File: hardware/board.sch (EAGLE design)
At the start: 45 parts, among them IC1 0915BM15A0001, J1 U.FL, U3 BLE113-A, X1 26MHz 10pF 10ppm -20C +70C, X3 MINI-USB-UX60-MB-5ST

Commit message: Update parts for 24MHz in schematic and BOM
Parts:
- C5, C6: value 27pF -> 11pF
- X1: value 26MHz 10pF 10ppm -20C +70C -> 24MHz 8pF 10ppm -20C +70C
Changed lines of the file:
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@@
 <?xml version="1.0" encoding="utf-8"?>
 <!DOCTYPE eagle SYSTEM "eagle.dtd">
-<eagle version="7.1.0">
+<eagle version="7.4.0">
 <drawing>
 <settings>
@@
 <parts>
 <part name="CC1110" library="parts" deviceset="CC1110" device=""/>
-<part name="X1" library="cts_crystal" deviceset="CTS_32X25_SMD" device="" value="26MHz 10pF 10ppm -20C +70C"/>
+<part name="X1" library="cts_crystal" deviceset="CTS_32X25_SMD" device="" value="24MHz 8pF 10ppm -20C +70C"/>
 <part name="C1" library="rcl" deviceset="C-EU" device="C0402" value="100nF"/>
 <part name="SUPPLY4" library="supply2" deviceset="GND" device=""/>
@@
 <part name="J1" library="SparkFun-Connectors" deviceset="U.FL" device="" value="U.FL"/>
 <part name="U3" library="sf-bluegiga" deviceset="BLE113" device="-A"/>
-<part name="C5" library="rcl" deviceset="C-EU" device="C0402K" value="27pF"/>
-<part name="C6" library="rcl" deviceset="C-EU" device="C0402K" value="27pF"/>
+<part name="C5" library="rcl" deviceset="C-EU" device="C0402K" value="11pF"/>
+<part name="C6" library="rcl" deviceset="C-EU" device="C0402K" value="11pF"/>
 <part name="GND15" library="supply1" deviceset="GND" device=""/>
 <part name="GND16" library="supply1" deviceset="GND" device=""/>

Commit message: Update loading cap specifications to 12pF
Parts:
- C5, C6: value 11pF -> 12pF ±5%
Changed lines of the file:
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@@
 <part name="J1" library="SparkFun-Connectors" deviceset="U.FL" device="" value="U.FL"/>
 <part name="U3" library="sf-bluegiga" deviceset="BLE113" device="-A"/>
-<part name="C5" library="rcl" deviceset="C-EU" device="C0402K" value="11pF"/>
-<part name="C6" library="rcl" deviceset="C-EU" device="C0402K" value="11pF"/>
+<part name="C5" library="rcl" deviceset="C-EU" device="C0402K" value="12pF ±5%"/>
+<part name="C6" library="rcl" deviceset="C-EU" device="C0402K" value="12pF ±5%"/>
 <part name="GND15" library="supply1" deviceset="GND" device=""/>
 <part name="GND16" library="supply1" deviceset="GND" device=""/>

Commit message: Fix decoupling cap; it was an error to have it so big. Also, the Digikey BOM had a mistake for its part number.
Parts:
- C11: value 100uF -> 10uF
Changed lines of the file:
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@@
 <part name="SUPPLY19" library="supply2" deviceset="GND" device=""/>
 <part name="SUPPLY20" library="supply2" deviceset="GND" device=""/>
-<part name="C11" library="rcl" deviceset="C-US" device="C0805K" value="100uF"/>
+<part name="C11" library="rcl" deviceset="C-US" device="C0805K" value="10uF"/>
 <part name="SUPPLY15" library="supply2" deviceset="GND" device=""/>
 <part name="SUPPLY18" library="supply2" deviceset="VDD" device=""/>

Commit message: reduce amount of solder under cc1110, and label board 0.7p for production run
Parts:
- CC1110: device parts:CC1110 -> board:CC1110
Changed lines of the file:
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@@
 </classes>
 <parts>
-<part name="CC1110" library="parts" deviceset="CC1110" device=""/>
+<part name="CC1110" library="board" deviceset="CC1110" device=""/>
 <part name="X1" library="cts_crystal" deviceset="CTS_32X25_SMD" device="" value="24MHz 8pF 10ppm -20C +70C"/>
 <part name="C1" library="rcl" deviceset="C-EU" device="C0402" value="100nF"/>

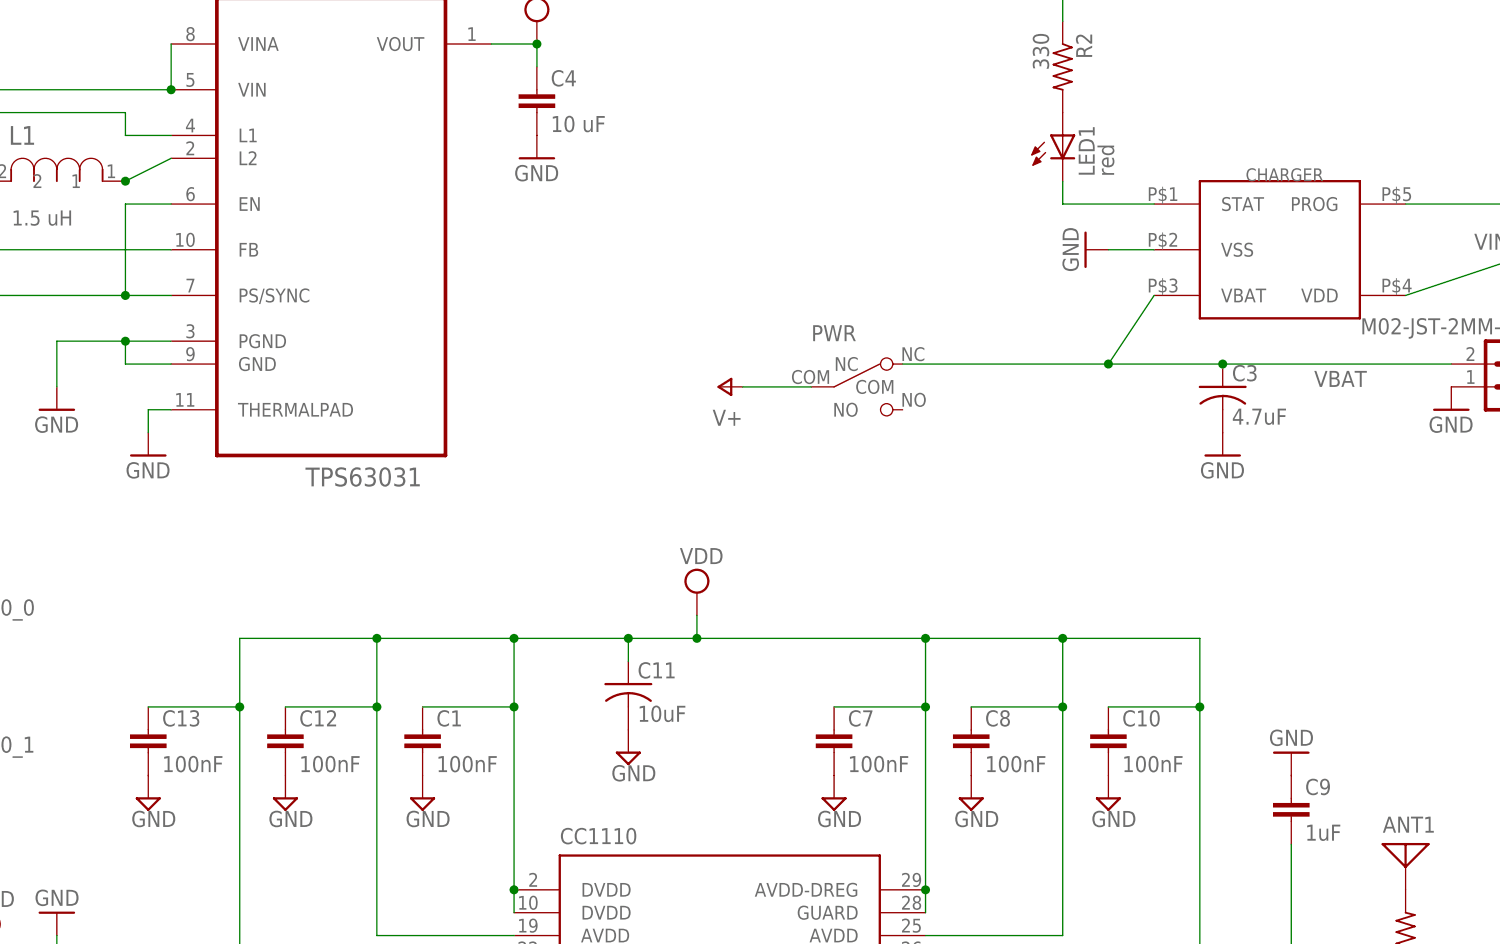
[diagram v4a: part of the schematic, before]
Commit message: Map all parts to digikey part numbers, unify part names and descriptions.
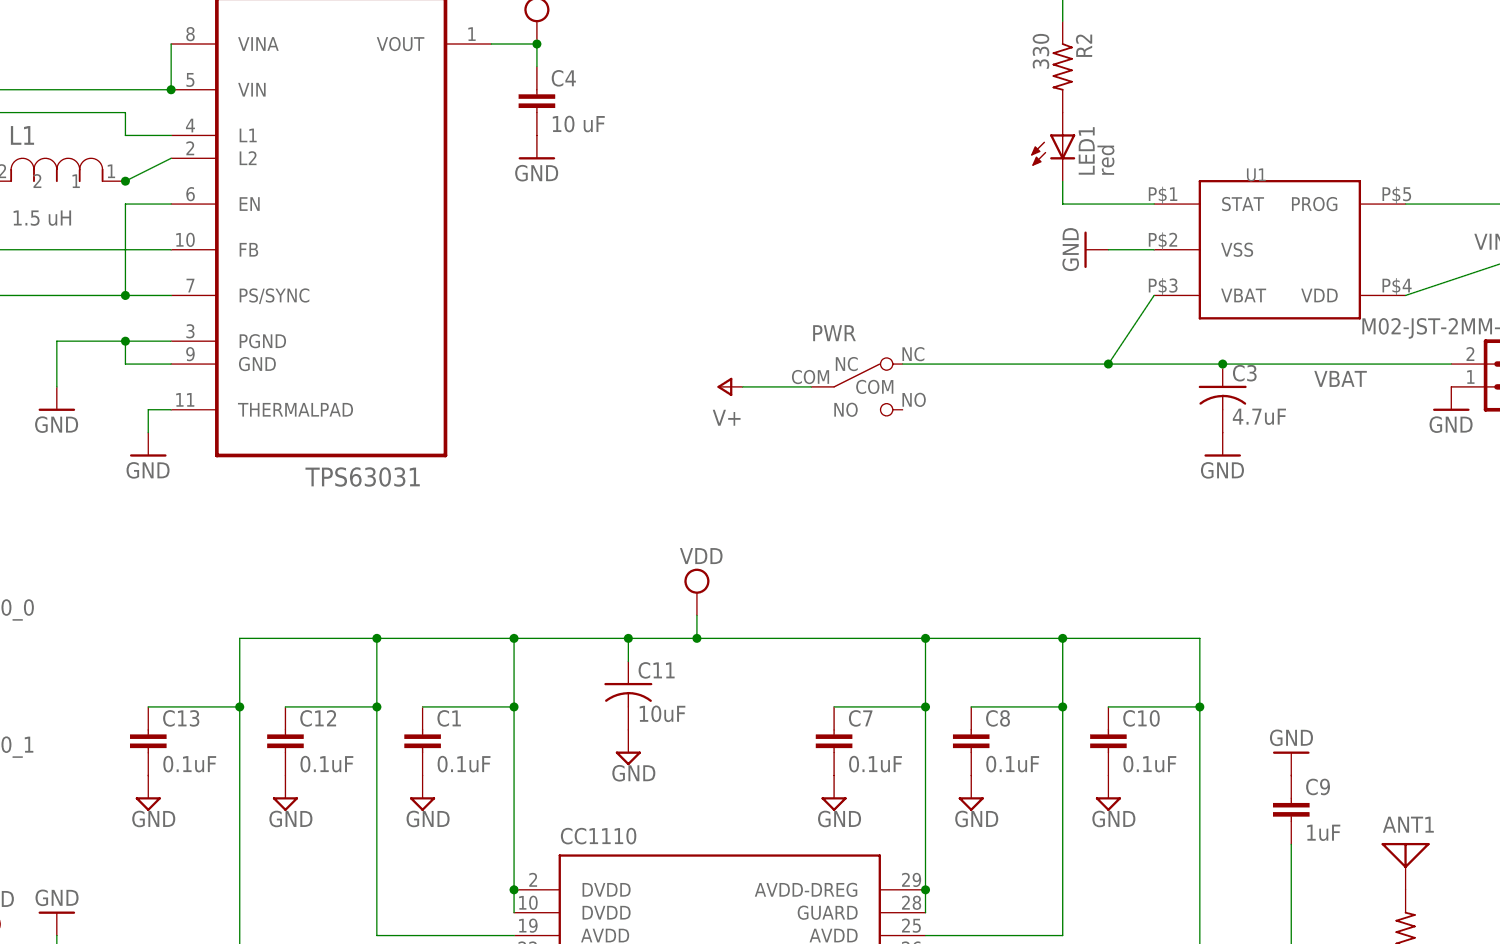
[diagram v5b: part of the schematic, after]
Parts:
- C1, C10, C12, C13, C7, C8: value 100nF -> 0.1uF
- renumbered CHARGER to U1
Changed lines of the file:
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@@
 <part name="CC1110" library="board" deviceset="CC1110" device=""/>
 <part name="X1" library="cts_crystal" deviceset="CTS_32X25_SMD" device="" value="24MHz 8pF 10ppm -20C +70C"/>
-<part name="C1" library="rcl" deviceset="C-EU" device="C0402" value="100nF"/>
+<part name="C1" library="rcl" deviceset="C-EU" device="C0402" value="0.1uF"/>
 <part name="SUPPLY4" library="supply2" deviceset="GND" device=""/>
 <part name="SUPPLY1" library="supply2" deviceset="VDD" device=""/>
-<part name="CHARGER" library="parts" deviceset="MCP73831" device=""/>
+<part name="U1" library="parts" deviceset="MCP73831" device=""/>
 <part name="X3" library="con-hirose" deviceset="MINI-USB-" device="UX60-MB-5ST"/>
 <part name="JP1" library="SparkFun-Connectors" deviceset="M02" device="-JST-2MM-SMT"/>
@@
 <part name="LED3" library="led" deviceset="LED" device="SML0603" value="green"/>
 <part name="R13" library="rcl" deviceset="R-US_" device="R0402" value="470 ohms"/>
-<part name="C7" library="rcl" deviceset="C-EU" device="C0402" value="100nF"/>
-<part name="C12" library="rcl" deviceset="C-EU" device="C0402" value="100nF"/>
+<part name="C7" library="rcl" deviceset="C-EU" device="C0402" value="0.1uF"/>
+<part name="C12" library="rcl" deviceset="C-EU" device="C0402" value="0.1uF"/>
 <part name="SUPPLY14" library="supply2" deviceset="GND" device=""/>
-<part name="C8" library="rcl" deviceset="C-EU" device="C0402" value="100nF"/>
+<part name="C8" library="rcl" deviceset="C-EU" device="C0402" value="0.1uF"/>
 <part name="SUPPLY16" library="supply2" deviceset="GND" device=""/>
-<part name="C10" library="rcl" deviceset="C-EU" device="C0402" value="100nF"/>
+<part name="C10" library="rcl" deviceset="C-EU" device="C0402" value="0.1uF"/>
 <part name="SUPPLY17" library="supply2" deviceset="GND" device=""/>
-<part name="C13" library="rcl" deviceset="C-EU" device="C0402" value="100nF"/>
+<part name="C13" library="rcl" deviceset="C-EU" device="C0402" value="0.1uF"/>
 <part name="SUPPLY19" library="supply2" deviceset="GND" device=""/>
 <part name="SUPPLY20" library="supply2" deviceset="GND" device=""/>
@@
 <instance part="SUPPLY4" gate="GND" x="43.18" y="88.9"/>
 <instance part="SUPPLY1" gate="G$1" x="73.66" y="111.76"/>
-<instance part="CHARGER" gate="G$1" x="137.16" y="149.86"/>
+<instance part="U1" gate="G$1" x="137.16" y="149.86"/>
 <instance part="X3" gate="G$1" x="185.42" y="177.8"/>
 <instance part="JP1" gate="G$1" x="165.1" y="137.16" rot="R180"/>
@@
 </segment>
 <segment>
-<pinref part="CHARGER" gate="G$1" pin="VSS"/>
+<pinref part="U1" gate="G$1" pin="VSS"/>
 <pinref part="GND4" gate="1" pin="GND"/>
 <wire x1="124.46" y1="149.86" x2="119.38" y2="149.86" width="0.1524" layer="91"/>
@@
 <net name="N$3" class="0">
 <segment>
-<pinref part="CHARGER" gate="G$1" pin="PROG"/>
+<pinref part="U1" gate="G$1" pin="PROG"/>
 <wire x1="152.4" y1="154.94" x2="167.64" y2="154.94" width="0.1524" layer="91"/>
 <pinref part="R1" gate="G$1" pin="2"/>
@@
 <net name="N$2" class="0">
 <segment>
-<pinref part="CHARGER" gate="G$1" pin="STAT"/>
+<pinref part="U1" gate="G$1" pin="STAT"/>
 <pinref part="LED1" gate="G$1" pin="C"/>
 <wire x1="124.46" y1="154.94" x2="114.3" y2="154.94" width="0.1524" layer="91"/>
@@
 <net name="VIN_USB" class="0">
 <segment>
-<pinref part="CHARGER" gate="G$1" pin="VDD"/>
+<pinref part="U1" gate="G$1" pin="VDD"/>
 <pinref part="C2" gate="G$1" pin="1"/>
 <wire x1="175.26" y1="152.4" x2="152.4" y2="144.78" width="0.1524" layer="91"/>
@@
 <net name="VBAT" class="0">
 <segment>
-<pinref part="CHARGER" gate="G$1" pin="VBAT"/>
+<pinref part="U1" gate="G$1" pin="VBAT"/>
 <wire x1="124.46" y1="144.78" x2="119.38" y2="137.16" width="0.1524" layer="91"/>
 <pinref part="C3" gate="G$1" pin="1"/>

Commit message: Update placement marks to show part orientation
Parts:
- REGULATOR: device Texas Instruments_By_element14_Batch_1:TPS63031 -> board:TPS63031
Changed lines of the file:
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@@
 <part name="GND5" library="supply1" deviceset="GND" device=""/>
 <part name="GND6" library="supply1" deviceset="GND" device=""/>
-<part name="REGULATOR" library="Texas Instruments_By_element14_Batch_1" deviceset="TPS63031" device="">
+<part name="REGULATOR" library="board" deviceset="TPS63031" device="">
 <attribute name="MPN" value="TPS63031"/>
 </part>
